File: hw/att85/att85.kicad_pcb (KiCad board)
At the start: 2 copper layers, 80 x 40 mm, 37 parts, among them J101 Barrel_Jack_Switch, J102 Screw_Terminal_01x03, J103 AVR-ISP-6, J104 Conn_01x02, J105 Conn_01x02, Q101 BC817, SW101 SW_Push, SW102 SW_Push, SW103 SW_Push, SW104 SW_Push, SW105 SW_Push, SW106 SW_Push, U101 ATtiny85-20P, U102 MT3608-MODULE

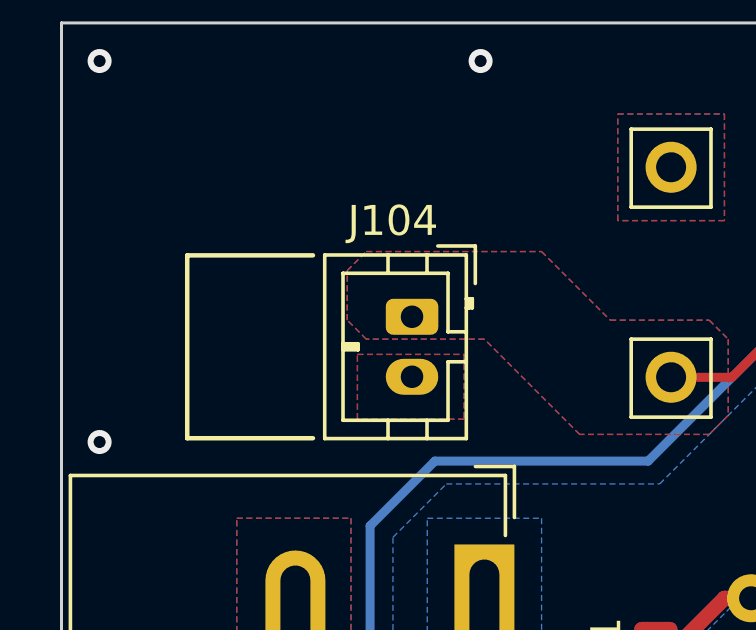
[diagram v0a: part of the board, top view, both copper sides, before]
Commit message: chore(hw): move battery connector
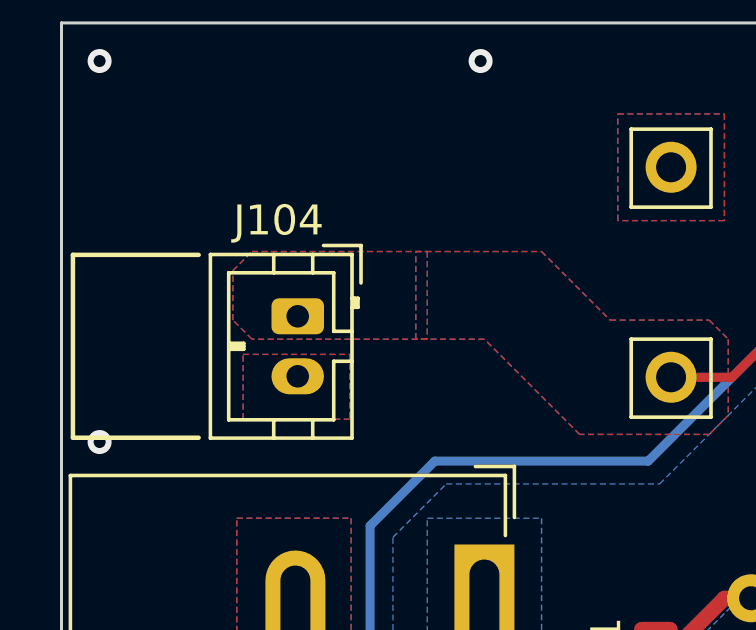
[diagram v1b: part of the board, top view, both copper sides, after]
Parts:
- moved J104 3.81 mm to (127.3, 84.7)
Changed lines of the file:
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@@
   )
   (footprint "Connector_JST:JST_PH_B2B-PH-K_1x02_P2.00mm_Vertical" (layer "F.Cu")
-    (at 131.064 84.725 -90)
+    (at 127.254 84.709 -90)
     (descr "JST PH series connector, B2B-PH-K (http://www.jst-mfg.com/product/pdf/eng/ePH.pdf), generated with kicad-footprint-generator")
     (tags "connector JST PH side entry")
@@
     )
     (stroke (width 0.15) (type solid)) (fill solid) (layer "F.SilkS"))
-  (gr_line (start 123.571 88.773) (end 127.762 88.773)
+  (gr_line (start 119.761 88.757) (end 123.952 88.757)
     (stroke (width 0.15) (type default)) (layer "F.SilkS"))
   (gr_line (start 184.404 106.68) (end 183.134 105.41)
@@
     )
     (stroke (width 0.15) (type solid)) (fill solid) (layer "F.SilkS"))
-  (gr_line (start 127.762 82.677) (end 123.571 82.677)
+  (gr_line (start 123.952 82.661) (end 119.761 82.661)
     (stroke (width 0.15) (type default)) (layer "F.SilkS"))
   (gr_poly
@@
     )
     (stroke (width 0.15) (type solid)) (fill solid) (layer "F.SilkS"))
-  (gr_line (start 123.571 82.677) (end 123.571 88.773)
+  (gr_line (start 119.761 82.661) (end 119.761 88.757)
     (stroke (width 0.15) (type default)) (layer "F.SilkS"))
   (gr_circle (center 147.828 106.045) (end 148.463 106.045)
@@
     (polygon
       (pts
-        (xy 129.244 85.979)
-        (xy 132.8 85.979)
-        (xy 132.8 88.138)
-        (xy 129.244 88.138)
+        (xy 125.434 85.979)
+        (xy 128.99 85.979)
+        (xy 128.99 88.138)
+        (xy 125.434 88.138)
       )
     )
@@
     (polygon
       (pts
-        (xy 129.54 85.471)
-        (xy 128.905 84.836)
-        (xy 128.905 83.185)
-        (xy 129.54 82.55)
+        (xy 131.191 85.471)
+        (xy 131.191 82.55)
         (xy 135.382 82.55)
         (xy 137.668 84.836)
@@
         (xy 196.469 101.727)
         (xy 191.897 101.727)
+      )
+    )
+  )
+  (zone (net 23) (net_name "Net-(J104-Pin_1)") (layers "F&B.Cu") (hatch edge 0.5)
+    (priority 6)
+    (connect_pads (clearance 0.5))
+    (min_thickness 0.25) (filled_areas_thickness no)
+    (fill yes (thermal_gap 0.5) (thermal_bridge_width 1))
+    (polygon
+      (pts
+        (xy 125.73 85.471)
+        (xy 125.095 84.836)
+        (xy 125.095 83.185)
+        (xy 125.73 82.55)
+        (xy 131.572 82.55)
+        (xy 131.572 85.471)
       )
     )
@@
     )
   )
+  (group "" (id 7b88d908-90d5-4975-a826-fd0900ca3e9e)
+    (members
+      8ea197c1-39c9-483f-9f82-17212adb1ab0
+      d4fc0b85-1f47-4264-8a48-00686289e97f
+      d8d63569-22b7-4bbf-9669-7150fa93556c
+    )
+  )

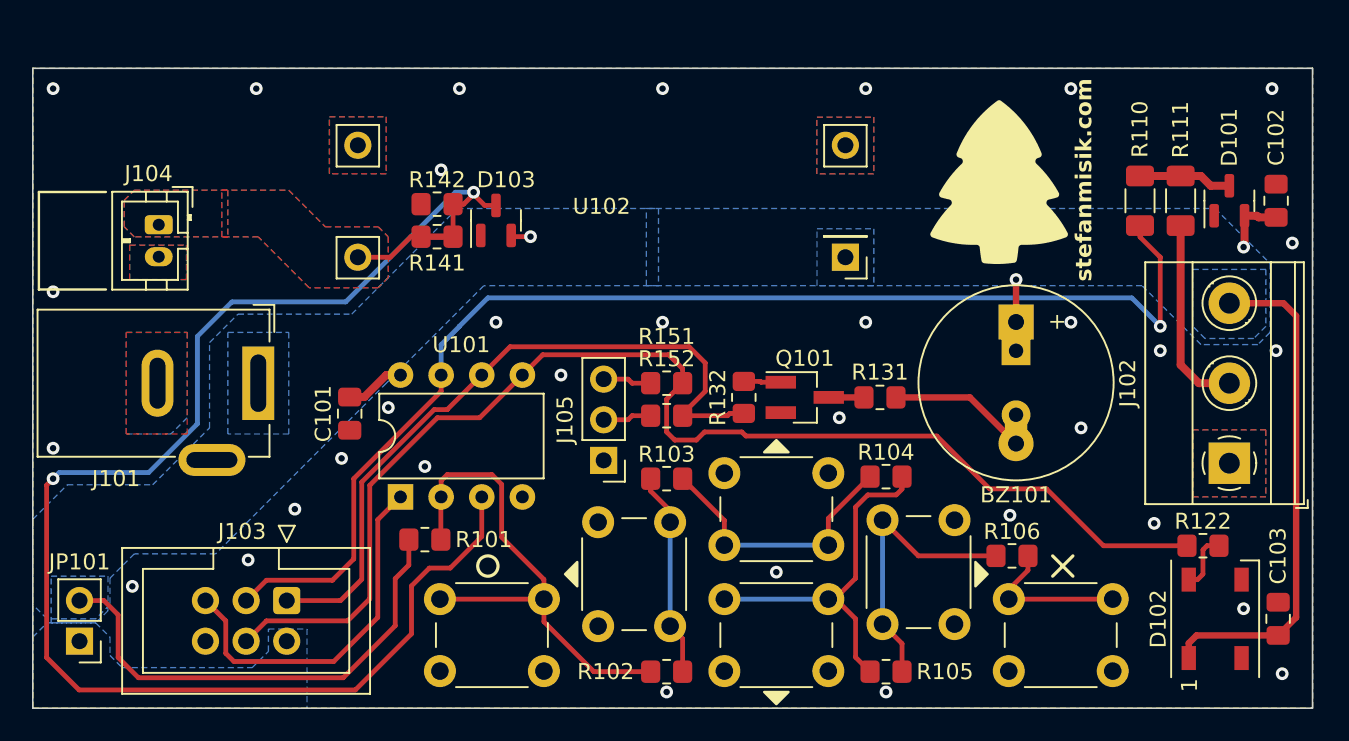
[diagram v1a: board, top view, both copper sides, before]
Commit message: feat(hw): add IR receiver
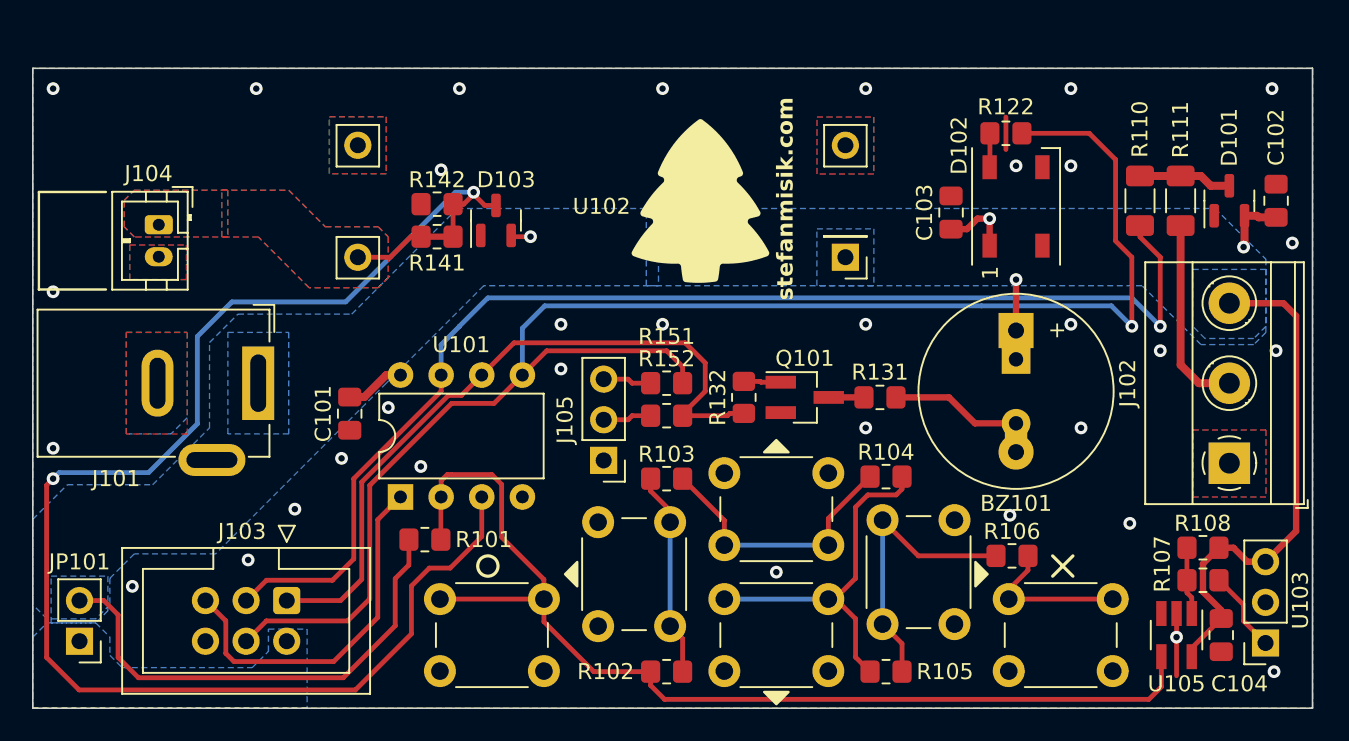
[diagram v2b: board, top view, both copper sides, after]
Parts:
- added C104: 100n, Capacitor_SMD:C_0805_2012Metric_Pad1.18x1.45mm_HandSolder, F.Cu at (193.7, 110.4)
- added R107: 47R, Resistor_SMD:R_0805_2012Metric_Pad1.20x1.40mm_HandSolder, F.Cu at (192.5, 106.9)
- added R108: 10K, Resistor_SMD:R_0805_2012Metric_Pad1.20x1.40mm_HandSolder, F.Cu at (192.5, 104.9)
- added U103: ~, Connector_PinSocket_2.54mm:PinSocket_1x03_P2.54mm_Vertical, F.Cu at (196.4, 110.9)
- added U105: 74AHC1G125, Package_TO_SOT_SMD:SOT-23-5_HandSoldering, F.Cu at (190.9, 110.4)
- moved C103 32.6 mm to (176.8, 83.9)
- moved D102 28.6 mm to (180.8, 83.6)
- moved R122 28.6 mm to (180.2, 79.0), turned to 180 degrees
- moved BZ101 0.53 mm to (180.8, 91.3)
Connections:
- net /KEYPAD_ADC renamed /KEYPAD_ADC/IR
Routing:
- net /KEYPAD_ADC/IR: track 32.0 -> 67.4 mm
- net /STATUS_LED/MOSI: track 79.5 -> 99.9 mm, vias 0 -> 1
- net GND: track 0.05 -> 5.97 mm
- net +5V: track 73.7 -> 79.3 mm, vias 3 -> 4
- net Net-(U103-OUT): track 0.00 -> 5.13 mm
- net Net-(R107-Pad1): track 0.00 -> 4.23 mm
- net Net-(D102-DIN): track 3.66 -> 2.13 mm
- net Net-(BZ101--): track 8.70 -> 8.18 mm

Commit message: chore(hw): improve layout
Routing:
- net GND: vias 33 -> 34

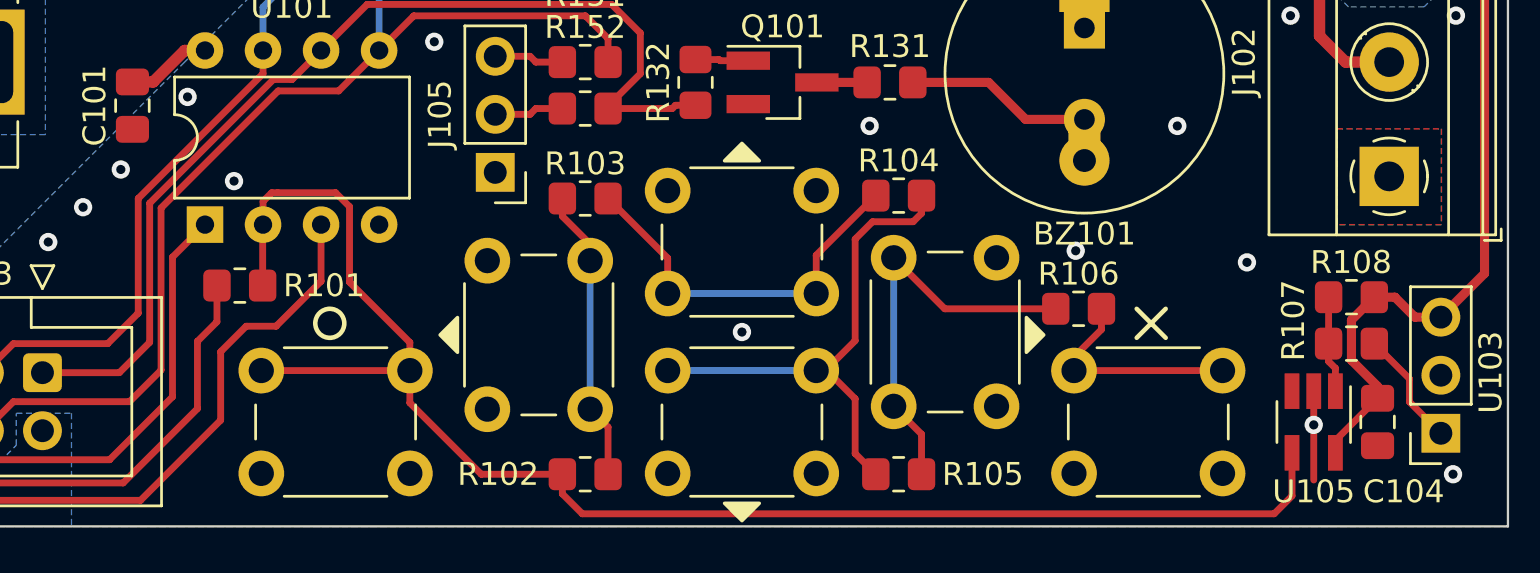
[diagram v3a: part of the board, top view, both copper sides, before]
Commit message: chore(hw): add separate divider position for IR receiver
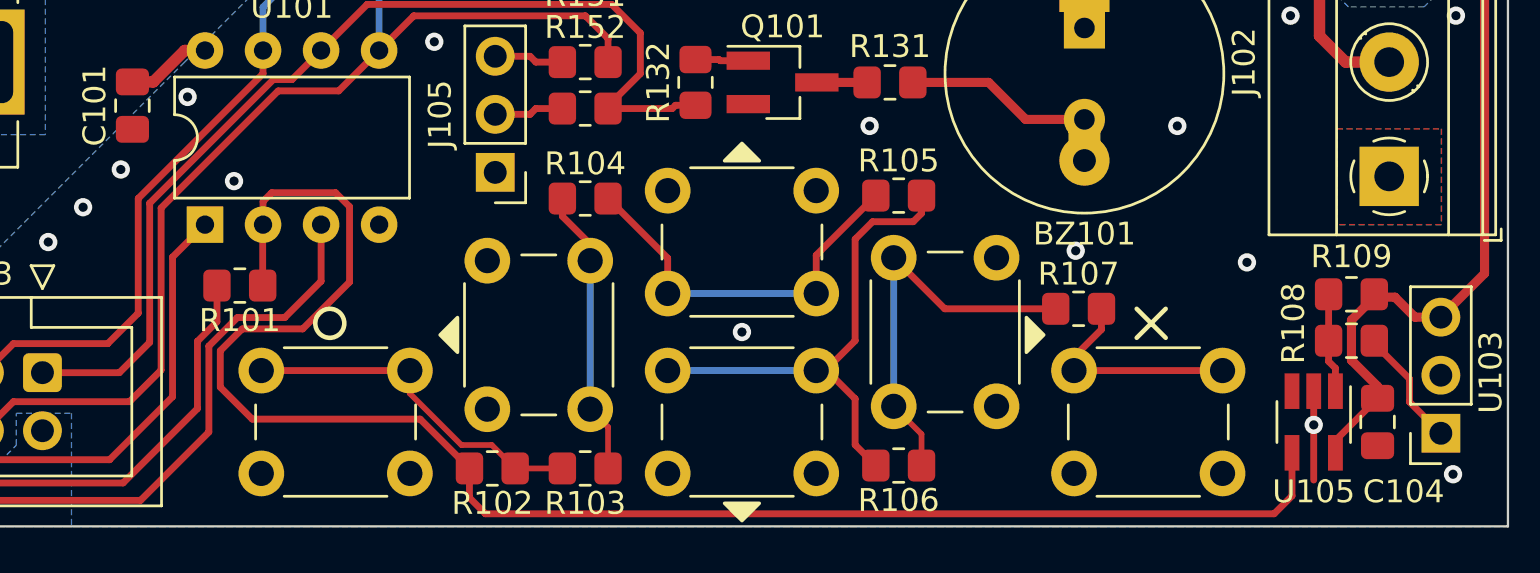
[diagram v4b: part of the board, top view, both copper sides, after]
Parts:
- added R109: 10K, Resistor_SMD:R_0805_2012Metric_Pad1.20x1.40mm_HandSolder, F.Cu at (192.5, 104.8)
- R102: value 470R -> 330R
- R103: value 680R -> 470R
- R104: value 1K -> 680R
- R105: value 2K -> 1K
- R106: value 7K5 -> 2K
- R107: value 47R -> 7K5
- R108: value 10K -> 47R
- moved R104 13.7 mm to (159.0, 100.6)
- moved R105 12.2 mm to (172.7, 100.5)
- moved R107 12.0 mm to (180.6, 105.4)
- moved R103 11.8 mm to (159.0, 112.4)
- moved R106 10.4 mm to (172.7, 112.3)
- moved R102 4.07 mm to (154.9, 112.4)
- moved R108 1.91 mm to (192.5, 106.8)
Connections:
- R107 pad 1: Net-(R107-Pad1) -> Net-(R106-Pad2)
- R107 pad 2: Net-(U103-OUT) -> Net-(R107-Pad2)
- R108 pad 1: Net-(R107-Pad1) -> Net-(R108-Pad1)
- R108 pad 2: +5V -> Net-(U103-OUT)
- SW101 pad 2: /KEYPAD_ADC/IR -> Net-(R102-Pad2)
- SW102 pad 2: Net-(R102-Pad2) -> Net-(R103-Pad2)
- SW103 pad 2: Net-(R103-Pad2) -> Net-(R104-Pad2)
- SW104 pad 2: Net-(R104-Pad2) -> Net-(R105-Pad2)
- SW105 pad 2: Net-(R105-Pad2) -> Net-(R106-Pad2)
- SW106 pad 2: Net-(R106-Pad2) -> Net-(R107-Pad2)
- U105 pad 1: Net-(R107-Pad1) -> Net-(R108-Pad1)
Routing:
- net Net-(R107-Pad2): track 0.00 -> 9.70 mm
- net Net-(R106-Pad2): track 9.70 -> 17.6 mm
- net Net-(R104-Pad2): track 23.2 -> 17.1 mm
- net Net-(R105-Pad2): track 18.0 -> 22.8 mm
- net Net-(R103-Pad2): track 17.1 -> 12.6 mm
- net /KEYPAD_ADC/IR: track 67.4 -> 71.8 mm
- net Net-(R108-Pad1): track 0.00 -> 4.23 mm
- net Net-(R107-Pad1): track 4.23 -> 0.00 mm
- net Net-(R102-Pad2): track 12.9 -> 15.5 mm

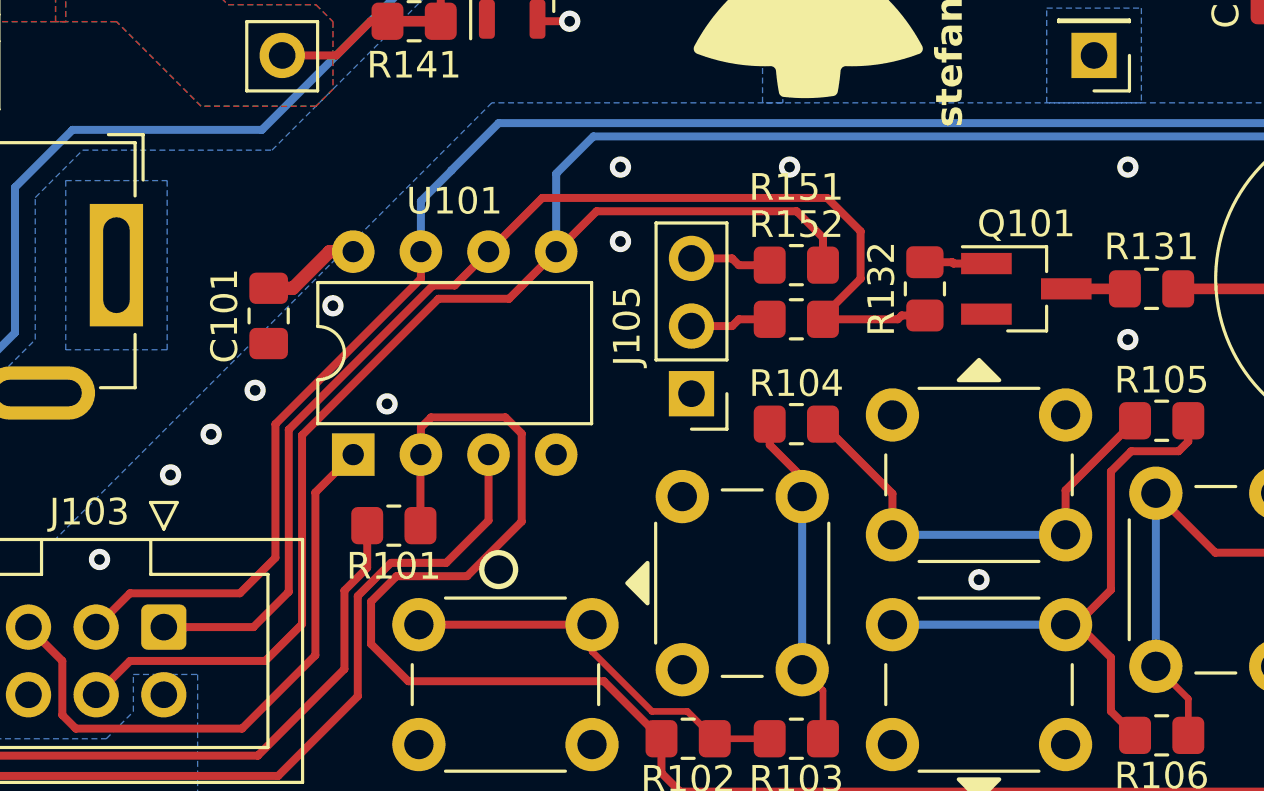
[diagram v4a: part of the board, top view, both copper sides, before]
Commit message: chore(hw): remove UART RX, allow buzzer to be disconnected
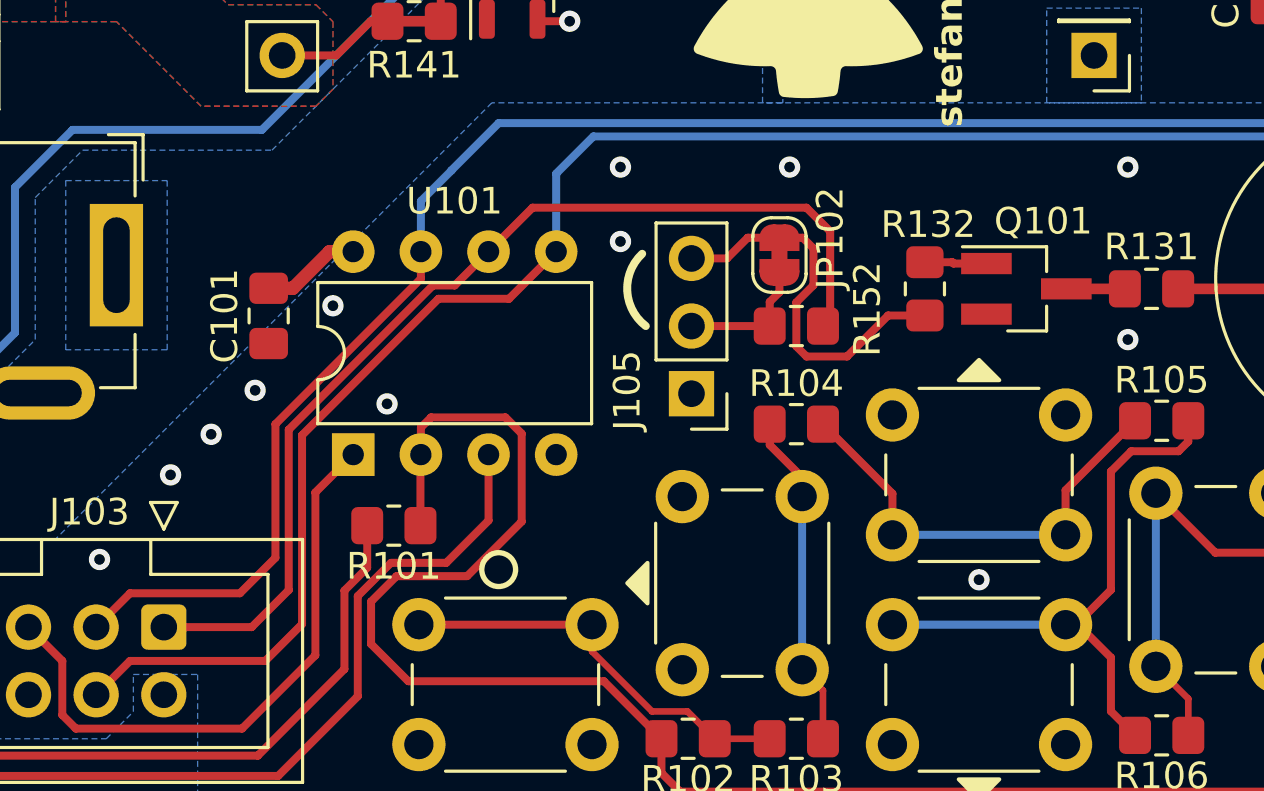
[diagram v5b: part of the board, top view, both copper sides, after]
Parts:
- removed R151: 330R, Resistor_SMD:R_0805_2012Metric_Pad1.20x1.40mm_HandSolder
- added JP102: Jumper_2_Bridged, Jumper:SolderJumper-2_P1.3mm_Bridged_RoundedPad1.0x1.5mm, F.Cu at (158.4, 94.2)
- moved R152 0.25 mm to (159.0, 96.9), turned to 0 degrees
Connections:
- J103 pad 1: /BUZZER/MISO -> /BUZZER/TX/MISO
- J105 pad 3: Net-(J105-Pin_3) -> /BUZZER
- R132 pad 1: /BUZZER/MISO -> /BUZZER
- R152 pad 1: /BUZZER/MISO -> Net-(J105-Pin_2)
- R152 pad 2: Net-(J105-Pin_2) -> /BUZZER/TX/MISO
- U101 pad 6: /BUZZER/MISO -> /BUZZER/TX/MISO
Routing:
- net /BUZZER/MISO: track 44.7 -> 0.00 mm
- net /BUZZER/TX/MISO: track 0.00 -> 39.1 mm
- net /BUZZER: track 0.00 -> 14.6 mm
- net /STATUS_LED/MOSI: track 99.9 -> 87.8 mm
- net Net-(J105-Pin_3): track 3.04 -> 0.00 mm
- net Net-(J105-Pin_2): track 3.04 -> 5.11 mm
